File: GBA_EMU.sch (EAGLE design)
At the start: 100 parts, among them J1 USB-MINIB-5PIN, J2 AVR_SPI, SW1 LEFT, SW2 RIGHT, SW3 PWR_SWITCH, SW8 OS102011MA1Q, U1 MIC7221, U2 MCP1642B-ADJ, U4 LM4875, U5 Mic5365-2.8Y, U7 AZV321, X2 HEADPHONE

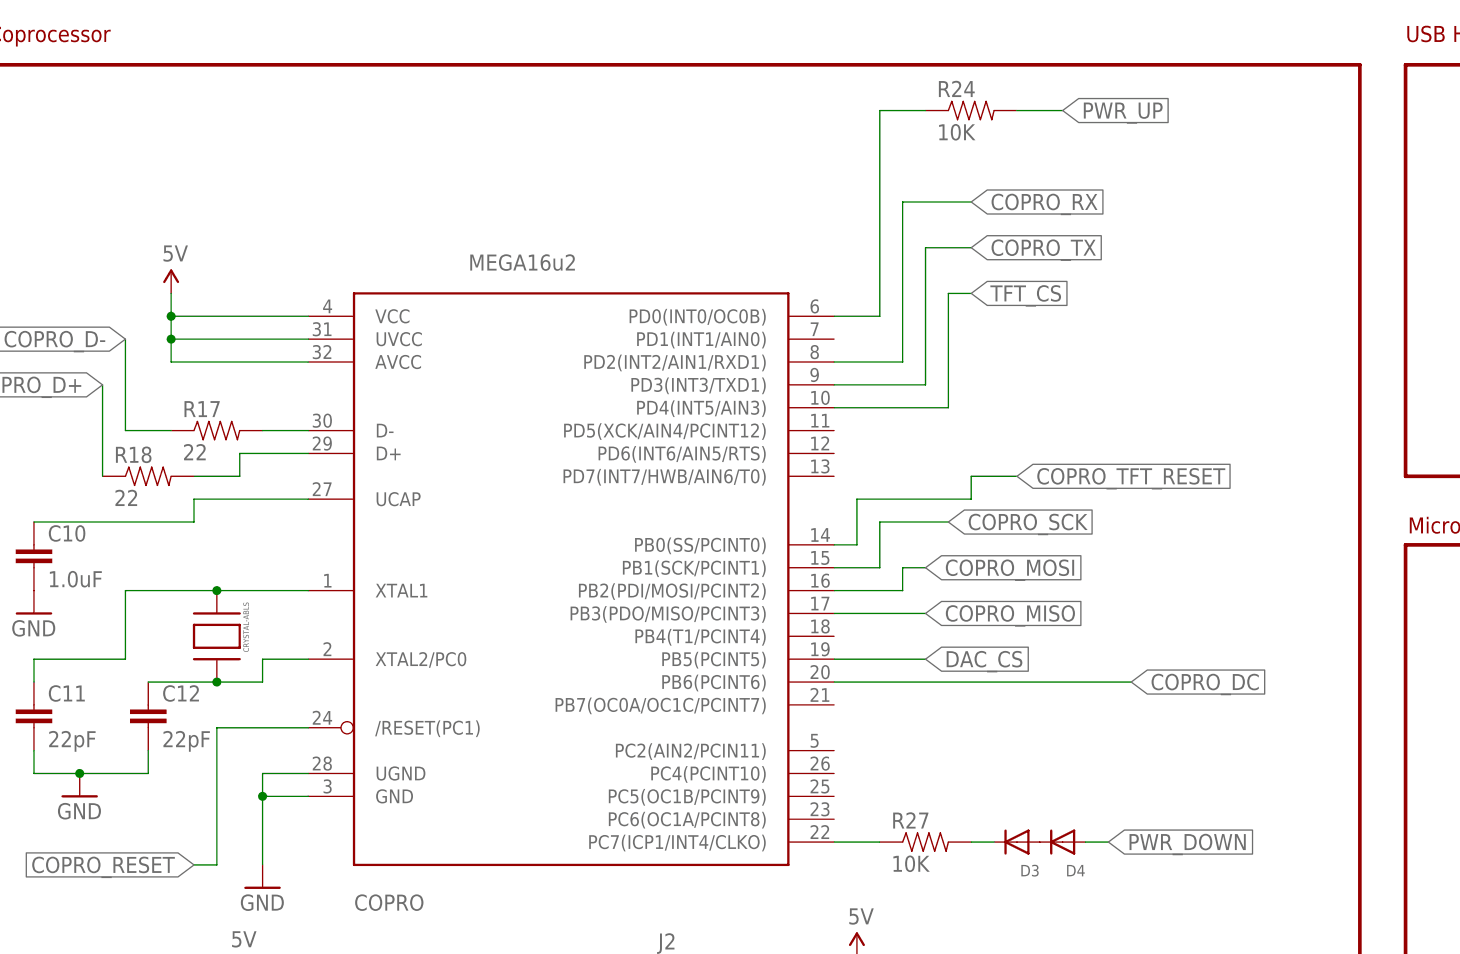
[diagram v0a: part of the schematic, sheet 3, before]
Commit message: switch to proprocessor to 3.3v
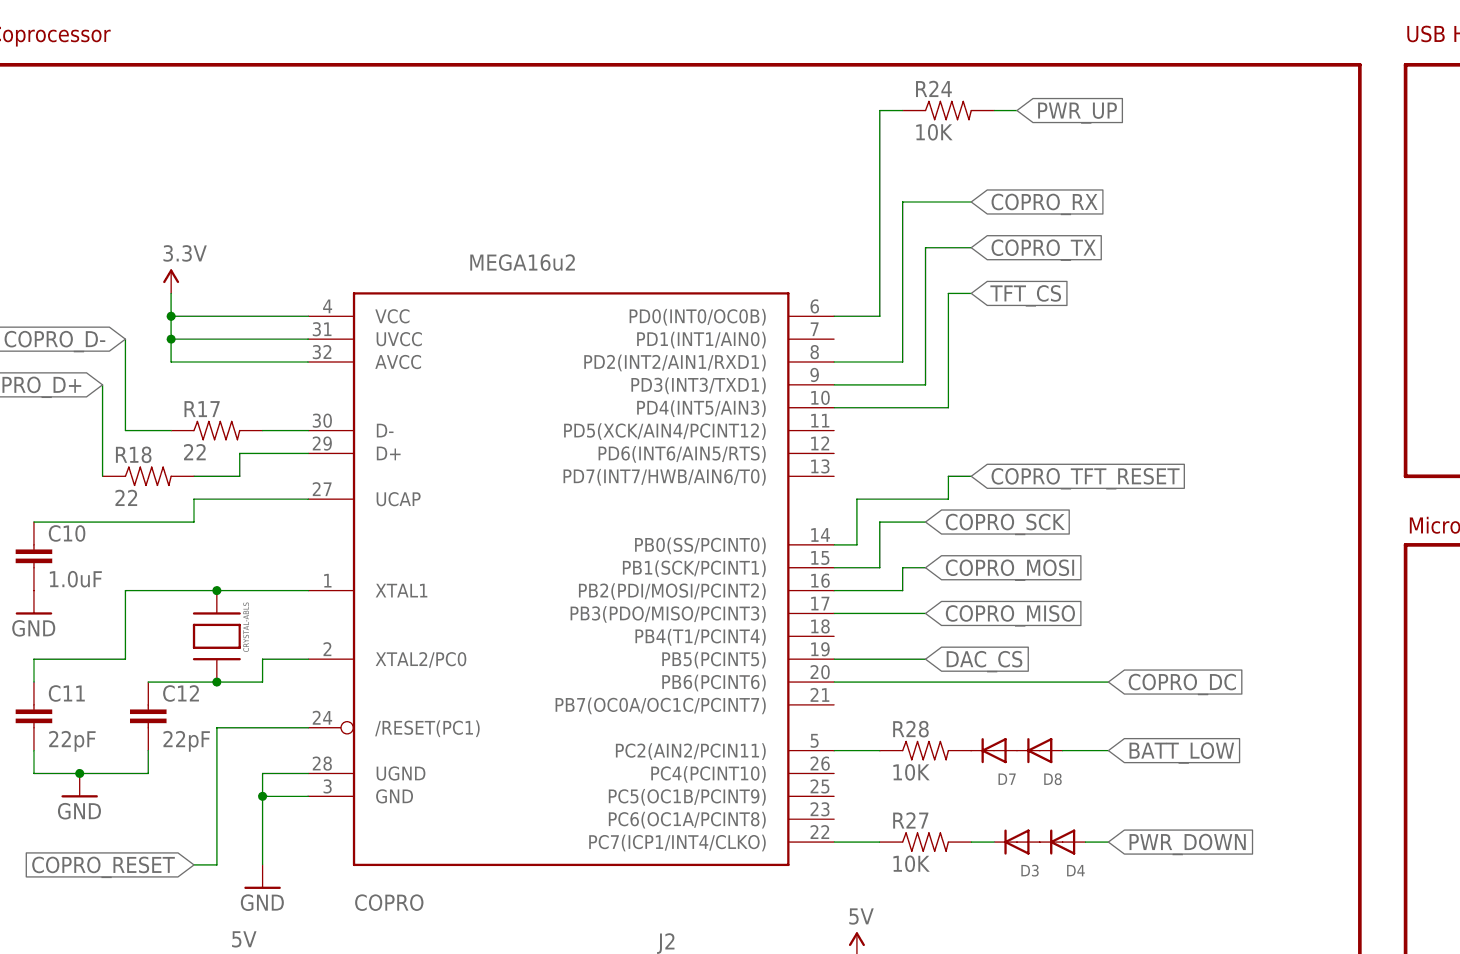
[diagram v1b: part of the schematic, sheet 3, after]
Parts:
- added D7, D8: (no value), adafruit:DIODESOD-523
- added R28: 10K, SparkFun-Resistors:10KOHM-1/10W-1%(0603)0603
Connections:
- new net BATT_LOW: D1.1, D1.3, D8.A, R3.2, U1.OUT1
- new net N$12: COPRO.PC2(AIN2/PCIN11), R28.1
- net 3.3V: now also COPRO.AVCC, COPRO.UVCC, COPRO.VCC
- net 5V: no longer COPRO.AVCC, COPRO.UVCC, COPRO.VCC
- net N$3: now also D7.A, D8.C; no longer D1.1, D1.3, R3.2, U1.OUT1
- net N$33: now also D7.C, R28.2
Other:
- moved on the sheet: R24
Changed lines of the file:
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@@
 <part name="SUPPLY12" library="SparkFun-Aesthetics" deviceset="5V" device=""/>
 <part name="R19" library="SparkFun-Resistors" deviceset="10KOHM-1/10W-1%(0603)" device="0603" value="10K"/>
-<part name="SUPPLY19" library="SparkFun-Aesthetics" deviceset="5V" device=""/>
 <part name="SUPPLY20" library="SparkFun-Aesthetics" deviceset="5V" device=""/>
 <part name="TP1" library="testpad" deviceset="PTR1" device="TP12R"/>
@@
 <part name="POT1" library="adafruit" deviceset="THUMBPOT" device=""/>
 <part name="SW8" library="adafruit" deviceset="OS102011MA1Q" device=""/>
+<part name="R28" library="SparkFun-Resistors" deviceset="10KOHM-1/10W-1%(0603)" device="0603" value="10K"/>
+<part name="D7" library="adafruit" deviceset="DIODE" device="SOD-523"/>
+<part name="D8" library="adafruit" deviceset="DIODE" device="SOD-523"/>
+<part name="SUPPLY19" library="SparkFun-Aesthetics" deviceset="3.3V" device=""/>
 </parts>
 <sheets>
@@
 </segment>
 </net>
-<net name="N$3" class="0">
+<net name="BATT_LOW" class="0">
 <segment>
 <pinref part="U1" gate="U$1" pin="OUT1"/>
@@
 <pinref part="D1" gate="D$1" pin="3"/>
 <junction x="523.24" y="179.07"/>
+<label x="490.22" y="177.8" size="1.778" layer="95" xref="yes"/>
 </segment>
 </net>
@@
 <instance part="SUPPLY12" gate="G$1" x="106.68" y="68.58"/>
 <instance part="R19" gate="G$1" x="38.1" y="58.42" rot="R90"/>
-<instance part="SUPPLY19" gate="G$1" x="30.48" y="142.24"/>
 <instance part="SUPPLY20" gate="G$1" x="38.1" y="66.04"/>
 <instance part="TP1" gate="G$1" x="22.86" y="27.94"/>
@@
 <instance part="GND38" gate="1" x="205.74" y="129.54"/>
 <instance part="SUPPLY38" gate="G$1" x="68.58" y="30.48"/>
-<instance part="R24" gate="G$1" x="119.38" y="162.56"/>
+<instance part="R24" gate="G$1" x="116.84" y="162.56"/>
 <instance part="D3" gate="G$1" x="124.46" y="81.28" rot="R180"/>
 <instance part="D4" gate="G$1" x="129.54" y="81.28" rot="R180"/>
 <instance part="R27" gate="G$1" x="114.3" y="81.28"/>
+<instance part="R28" gate="G$1" x="114.3" y="91.44"/>
+<instance part="D7" gate="G$1" x="121.92" y="91.44" rot="R180"/>
+<instance part="D8" gate="G$1" x="127" y="91.44" rot="R180"/>
+<instance part="SUPPLY19" gate="G$1" x="30.48" y="142.24"/>
 </instances>
 <busses>
@@
 <wire x1="104.14" y1="111.76" x2="109.22" y2="111.76" width="0.1524" layer="91"/>
 <wire x1="109.22" y1="111.76" x2="109.22" y2="116.84" width="0.1524" layer="91"/>
-<wire x1="109.22" y1="116.84" x2="116.84" y2="116.84" width="0.1524" layer="91"/>
-<label x="116.84" y="116.84" size="1.778" layer="95" xref="yes"/>
+<wire x1="109.22" y1="116.84" x2="114.3" y2="116.84" width="0.1524" layer="91"/>
+<label x="114.3" y="116.84" size="1.778" layer="95" xref="yes"/>
 </segment>
 <segment>
@@
 <wire x1="99.06" y1="66.04" x2="106.68" y2="66.04" width="0.1524" layer="91"/>
 <wire x1="106.68" y1="66.04" x2="106.68" y2="68.58" width="0.1524" layer="91"/>
+</segment>
+<segment>
+<pinref part="R19" gate="G$1" pin="2"/>
+<pinref part="SUPPLY20" gate="G$1" pin="5V"/>
+<wire x1="38.1" y1="66.04" x2="38.1" y2="63.5" width="0.1524" layer="91"/>
+</segment>
+<segment>
+<pinref part="TP1" gate="G$1" pin="TP"/>
+<pinref part="SUPPLY23" gate="G$1" pin="5V"/>
+</segment>
+<segment>
+<pinref part="X1" gate="G$1" pin="VBUS"/>
+<pinref part="SUPPLY31" gate="G$1" pin="5V"/>
+<wire x1="195.58" y1="149.86" x2="203.2" y2="149.86" width="0.1524" layer="91"/>
+<wire x1="203.2" y1="149.86" x2="203.2" y2="152.4" width="0.1524" layer="91"/>
+</segment>
+</net>
+<net name="3.3V" class="0">
+<segment>
+<pinref part="TP2" gate="G$1" pin="TP"/>
+<pinref part="SUPPLY24" gate="G$1" pin="3.3V"/>
 </segment>
 <segment>
@@
 <wire x1="30.48" y1="134.62" x2="30.48" y2="137.16" width="0.1524" layer="91"/>
 <junction x="30.48" y="137.16"/>
-<pinref part="SUPPLY19" gate="G$1" pin="5V"/>
-</segment>
-<segment>
-<pinref part="R19" gate="G$1" pin="2"/>
-<pinref part="SUPPLY20" gate="G$1" pin="5V"/>
-<wire x1="38.1" y1="66.04" x2="38.1" y2="63.5" width="0.1524" layer="91"/>
-</segment>
-<segment>
-<pinref part="TP1" gate="G$1" pin="TP"/>
-<pinref part="SUPPLY23" gate="G$1" pin="5V"/>
-</segment>
-<segment>
-<pinref part="X1" gate="G$1" pin="VBUS"/>
-<pinref part="SUPPLY31" gate="G$1" pin="5V"/>
-<wire x1="195.58" y1="149.86" x2="203.2" y2="149.86" width="0.1524" layer="91"/>
-<wire x1="203.2" y1="149.86" x2="203.2" y2="152.4" width="0.1524" layer="91"/>
-</segment>
-</net>
-<net name="3.3V" class="0">
-<segment>
-<pinref part="TP2" gate="G$1" pin="TP"/>
-<pinref part="SUPPLY24" gate="G$1" pin="3.3V"/>
+<pinref part="SUPPLY19" gate="G$1" pin="3.3V"/>
 </segment>
 </net>
@@
 <wire x1="104.14" y1="114.3" x2="106.68" y2="114.3" width="0.1524" layer="91"/>
 <wire x1="106.68" y1="114.3" x2="106.68" y2="119.38" width="0.1524" layer="91"/>
-<wire x1="106.68" y1="119.38" x2="119.38" y2="119.38" width="0.1524" layer="91"/>
-<wire x1="119.38" y1="119.38" x2="119.38" y2="121.92" width="0.1524" layer="91"/>
-<wire x1="119.38" y1="121.92" x2="124.46" y2="121.92" width="0.1524" layer="91"/>
-<label x="124.46" y="121.92" size="1.778" layer="95" xref="yes"/>
+<wire x1="106.68" y1="119.38" x2="116.84" y2="119.38" width="0.1524" layer="91"/>
+<wire x1="116.84" y1="119.38" x2="116.84" y2="121.92" width="0.1524" layer="91"/>
+<wire x1="116.84" y1="121.92" x2="119.38" y2="121.92" width="0.1524" layer="91"/>
+<label x="119.38" y="121.92" size="1.778" layer="95" xref="yes"/>
 </segment>
 </net>
@@
 <segment>
 <pinref part="COPRO" gate="G$1" pin="PB6(PCINT6)"/>
-<wire x1="104.14" y1="99.06" x2="137.16" y2="99.06" width="0.1524" layer="91"/>
-<label x="137.16" y="99.06" size="1.778" layer="95" xref="yes"/>
+<wire x1="104.14" y1="99.06" x2="134.62" y2="99.06" width="0.1524" layer="91"/>
+<label x="134.62" y="99.06" size="1.778" layer="95" xref="yes"/>
 </segment>
 </net>
@@
 <segment>
 <pinref part="R24" gate="G$1" pin="2"/>
-<wire x1="129.54" y1="162.56" x2="124.46" y2="162.56" width="0.1524" layer="91"/>
-<label x="129.54" y="162.56" size="1.778" layer="95" xref="yes"/>
+<wire x1="124.46" y1="162.56" x2="121.92" y2="162.56" width="0.1524" layer="91"/>
+<label x="124.46" y="162.56" size="1.778" layer="95" xref="yes"/>
 </segment>
 </net>
@@
 <wire x1="109.22" y1="139.7" x2="109.22" y2="162.56" width="0.1524" layer="91"/>
 <pinref part="R24" gate="G$1" pin="1"/>
-<wire x1="109.22" y1="162.56" x2="114.3" y2="162.56" width="0.1524" layer="91"/>
+<wire x1="109.22" y1="162.56" x2="111.76" y2="162.56" width="0.1524" layer="91"/>
 </segment>
 </net>
@@
 <wire x1="121.92" y1="81.28" x2="119.38" y2="81.28" width="0.1524" layer="91"/>
 </segment>
+<segment>
+<pinref part="D7" gate="G$1" pin="C"/>
+<pinref part="R28" gate="G$1" pin="2"/>
+</segment>
 </net>
 <net name="N$38" class="0">
@@
 </segment>
 </net>
+<net name="N$3" class="0">
+<segment>
+<pinref part="D7" gate="G$1" pin="A"/>
+<pinref part="D8" gate="G$1" pin="C"/>
+</segment>
+</net>
+<net name="BATT_LOW" class="0">
+<segment>
+<pinref part="D8" gate="G$1" pin="A"/>
+<wire x1="129.54" y1="91.44" x2="134.62" y2="91.44" width="0.1524" layer="91"/>
+<label x="134.62" y="91.44" size="1.778" layer="95" xref="yes"/>
+</segment>
+</net>
+<net name="N$12" class="0">
+<segment>
+<pinref part="COPRO" gate="G$1" pin="PC2(AIN2/PCIN11)"/>
+<pinref part="R28" gate="G$1" pin="1"/>
+<wire x1="104.14" y1="91.44" x2="109.22" y2="91.44" width="0.1524" layer="91"/>
+</segment>
+</net>
